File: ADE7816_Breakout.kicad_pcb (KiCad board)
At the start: 2 copper layers, 9 parts, among them J1 Barrel_Jack_Switch, J2 AudioJack3, J3 AudioJack3, J4 AudioJack3, J5 AudioJack3, J6 AudioJack3, J7 AudioJack3, J8 Conn_01x06_Male, U1 ADE7816ACPZ

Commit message: Start adding analog inputs and filters
Signed-off-by: Tisham Dhar <whatnickd@gmail.com>
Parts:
- added C1: 22n, Capacitor_SMD:C_0603_1608Metric, F.Cu at (119.1, 70.1)
- added C10: 22n, Capacitor_SMD:C_0603_1608Metric, F.Cu at (131.5, 42.2)
- added C11: 22n, Capacitor_SMD:C_0603_1608Metric, F.Cu at (127.5, 47.2)
- added C12: 22n, Capacitor_SMD:C_0603_1608Metric, F.Cu at (131.5, 44.7)
- added C13: 22n, Capacitor_SMD:C_0603_1608Metric, F.Cu at (135.5, 42.2)
- added C14: 22n, Capacitor_SMD:C_0603_1608Metric, F.Cu at (-2146.0, -2146.7)
- added C2: 22n, Capacitor_SMD:C_0603_1608Metric, F.Cu at (151.5, 93.9)
- added C3: 22n, Capacitor_SMD:C_0603_1608Metric, F.Cu at (123.1, 70.1)
- added C4: 22n, Capacitor_SMD:C_0603_1608Metric, F.Cu at (119.1, 72.6)
- added C5: 22n, Capacitor_SMD:C_0603_1608Metric, F.Cu at (151.5, 91.4)
- added C6: 22n, Capacitor_SMD:C_0603_1608Metric, F.Cu at (139.3, 85.8)
- added C7: 22n, Capacitor_SMD:C_0603_1608Metric, F.Cu at (155.5, 91.4)
- added C8: 22n, Capacitor_SMD:C_0603_1608Metric, F.Cu at (127.5, 42.2)
- added C9: 22n, Capacitor_SMD:C_0603_1608Metric, F.Cu at (127.5, 44.7)
- added R1: 4.8R, Resistor_SMD:R_0603_1608Metric, F.Cu at (123.4, 67.6)
- added R10: 1k, Resistor_SMD:R_0603_1608Metric, F.Cu at (119.1, 80.1)
- added R11: 1k, Resistor_SMD:R_0603_1608Metric, F.Cu at (127.1, 72.6)
- added R12: 1k, Resistor_SMD:R_0603_1608Metric, F.Cu at (155.5, 93.9)
- added R13: 100k, Resistor_SMD:R_0603_1608Metric_Pad1.05x0.95mm_HandSolder, F.Cu at (119.3, 67.6)
- added R14: 1k, Resistor_SMD:R_0603_1608Metric, F.Cu at (143.3, 85.8)
- added R15: 1k, Resistor_SMD:R_0603_1608Metric, F.Cu at (131.5, 47.2)
- added R16: 1k, Resistor_SMD:R_0603_1608Metric, F.Cu at (135.5, 44.7)
- added R17: 1k, Resistor_SMD:R_0603_1608Metric, F.Cu at (139.5, 42.2)
- added R18: 1k, Resistor_SMD:R_0603_1608Metric, F.Cu at (135.5, 47.2)
- added R19: 1k, Resistor_SMD:R_0603_1608Metric, F.Cu at (139.5, 44.7)
- added R2: 4.8R, Resistor_SMD:R_0603_1608Metric, F.Cu at (123.1, 72.6)
- added R20: 1k, Resistor_SMD:R_0603_1608Metric, F.Cu at (139.5, 47.2)
- added R21: 1k, Resistor_SMD:R_0603_1608Metric, F.Cu at (-2142.0, -2146.7)
- added R3: 4.8R, Resistor_SMD:R_0603_1608Metric, F.Cu at (119.1, 75.1)
- added R4: 4.8R, Resistor_SMD:R_0603_1608Metric, F.Cu at (127.1, 70.1)
- added R5: 4.8R, Resistor_SMD:R_0603_1608Metric, F.Cu at (119.1, 77.6)
- added R6: 4.8R, Resistor_SMD:R_0603_1608Metric, F.Cu at (127.4, 67.6)
- added R7: 1k, Resistor_SMD:R_0603_1608Metric, F.Cu at (139.3, 88.4)
- added R8: 1k, Resistor_SMD:R_0603_1608Metric, F.Cu at (131.5, 67.6)
- added R9: 1k, Resistor_SMD:R_0603_1608Metric, F.Cu at (123.1, 75.1)
- J1: value Barrel_Jack_Switch -> AudioJack3; footprint Connector_BarrelJack:BarrelJack_Horizontal -> Connector_Audio:Jack_3.5mm_CUI_SJ-3523-SMT_Horizontal
- J7: value AudioJack3 -> Barrel_Jack_Switch; footprint Connector_Audio:Jack_3.5mm_CUI_SJ-3523-SMT_Horizontal -> Connector_BarrelJack:BarrelJack_Horizontal
- J8: value Conn_01x06_Male -> Conn_01x10; footprint Connector_PinHeader_2.54mm:PinHeader_1x06_P2.54mm_Vertical -> Connector_PinHeader_2.54mm:PinHeader_1x10_P2.54mm_Vertical
- moved J8 54.9 mm to (157.7, 53.3)
- moved J5 40.3 mm to (101.6, 36.8), turned to 90 degrees
- moved J6 38.2 mm to (101.9, 100.3), turned to 90 degrees
- moved J3 33.1 mm to (101.6, 61.1), turned to 90 degrees
- moved J1 31.2 mm to (101.9, 76.0), turned to 90 degrees
- moved J4 25.3 mm to (101.6, 49.0), turned to 90 degrees
- moved J7 23.0 mm to (128.0, 93.2), turned to 90 degrees
- moved J2 16.8 mm to (101.9, 88.2), turned to 90 degrees
- moved U1 11.8 mm to (136.4, 56.6)
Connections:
- J2 pad R: Net-(J2-PadR) -> (no net)
- J2 pad S: Net-(J2-PadS) -> GNDA
- J3 pad R: Net-(J3-PadR) -> (no net)
- J3 pad S: Net-(J3-PadS) -> GNDA
- J4 pad R: Net-(J4-PadR) -> (no net)
- J4 pad S: Net-(J4-PadS) -> GNDA
- J5 pad R: Net-(J5-PadR) -> (no net)
- J5 pad S: Net-(J5-PadS) -> GNDA
- J6 pad R: Net-(J6-PadR) -> (no net)
- J6 pad S: Net-(J6-PadS) -> GNDA
- J8 pad 1: Net-(J8-Pad1) -> (no net)
- J8 pad 2: Net-(J8-Pad2) -> (no net)
- J8 pad 3: Net-(J8-Pad3) -> (no net)
- J8 pad 4: Net-(J8-Pad4) -> (no net)
- J8 pad 5: Net-(J8-Pad5) -> (no net)
- J8 pad 6: Net-(J8-Pad6) -> (no net)
- U1 pad 1: Net-(U1-Pad1) -> (no net)
- U1 pad 10: Net-(U1-Pad10) -> (no net)
- U1 pad 11: Net-(U1-Pad11) -> (no net)
- U1 pad 12: Net-(U1-Pad12) -> (no net)
- U1 pad 13: Net-(U1-Pad13) -> (no net)
- U1 pad 14: Net-(U1-Pad14) -> (no net)
- U1 pad 15: Net-(U1-Pad15) -> (no net)
- U1 pad 16: Net-(U1-Pad16) -> (no net)
- U1 pad 17: Net-(U1-Pad17) -> (no net)
- U1 pad 18: Net-(U1-Pad18) -> (no net)
- U1 pad 19: Net-(U1-Pad19) -> (no net)
- U1 pad 2: Net-(U1-Pad2) -> (no net)
- U1 pad 20: Net-(U1-Pad20) -> (no net)
- U1 pad 21: Net-(U1-Pad21) -> (no net)
- U1 pad 22: Net-(U1-Pad22) -> (no net)
- U1 pad 23: Net-(U1-Pad23) -> (no net)
- U1 pad 24: Net-(U1-Pad24) -> (no net)
- U1 pad 25: Net-(U1-Pad25) -> (no net)
- U1 pad 26: Net-(U1-Pad26) -> (no net)
- U1 pad 27: Net-(U1-Pad27) -> (no net)
- U1 pad 28: Net-(U1-Pad28) -> (no net)
- U1 pad 29: Net-(U1-Pad29) -> (no net)
- U1 pad 3: Net-(U1-Pad3) -> (no net)
- U1 pad 30: Net-(U1-Pad30) -> (no net)
- U1 pad 31: Net-(U1-Pad31) -> (no net)
- U1 pad 32: Net-(U1-Pad32) -> (no net)
- U1 pad 33: Net-(U1-Pad33) -> (no net)
- U1 pad 34: Net-(U1-Pad34) -> (no net)
- U1 pad 35: Net-(U1-Pad35) -> (no net)
- U1 pad 36: Net-(U1-Pad36) -> (no net)
- U1 pad 37: Net-(U1-Pad37) -> (no net)
- U1 pad 38: Net-(U1-Pad38) -> (no net)
- U1 pad 39: Net-(U1-Pad39) -> (no net)
- U1 pad 4: Net-(U1-Pad4) -> (no net)
- U1 pad 40: Net-(U1-Pad40) -> (no net)
- U1 pad 5: Net-(U1-Pad5) -> (no net)
- U1 pad 6: Net-(U1-Pad6) -> (no net)
- U1 pad 7: Net-(U1-Pad7) -> (no net)
- U1 pad 8: Net-(U1-Pad8) -> (no net)
- U1 pad 9: Net-(U1-Pad9) -> (no net)
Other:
- board outline added: 66 x 76.2 mm

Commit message: Add crystal load caps
Signed-off-by: Tisham Dhar <whatnickd@gmail.com>
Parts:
- added C15: 20p, Capacitor_SMD:C_0603_1608Metric, F.Cu at (128.1, 56.1)
- added C16: 20p, Capacitor_SMD:C_0603_1608Metric, F.Cu at (128.1, 58.6)
- added Y1: 16.384MHz, Crystal:Crystal_SMD_2520-4Pin_2.5x2.0mm, F.Cu at (123.9, 56.9)
- moved C14 3182.6 mm to (143.5, 64.0)
- moved R21 3182.6 mm to (147.5, 64.0)
- moved J8 3.57 mm to (158.0, 56.9)
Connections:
- J1 pad R: (no net) -> Net-(J1-PadR)
- J2 pad R: (no net) -> Net-(J2-PadR)
- J3 pad R: (no net) -> Net-(J3-PadR)
- J4 pad R: (no net) -> Net-(J4-PadR)
- J5 pad R: (no net) -> Net-(J5-PadR)
- J6 pad R: (no net) -> Net-(J6-PadR)
- J7 pad 3: (no net) -> Net-(J7-Pad3)
- J8 pad 1: (no net) -> Net-(J8-Pad1)
- J8 pad 10: (no net) -> Net-(J8-Pad10)
- J8 pad 2: (no net) -> Net-(J8-Pad2)
- J8 pad 3: (no net) -> Net-(J8-Pad3)
- J8 pad 4: (no net) -> Net-(J8-Pad4)
- J8 pad 5: (no net) -> Net-(J8-Pad5)
- J8 pad 6: (no net) -> Net-(J8-Pad6)
- J8 pad 7: (no net) -> Net-(J8-Pad7)
- J8 pad 8: (no net) -> Net-(J8-Pad8)
- J8 pad 9: (no net) -> Net-(J8-Pad9)
- U1 pad 1: (no net) -> Net-(U1-Pad1)
- U1 pad 10: (no net) -> Net-(U1-Pad10)
- U1 pad 11: (no net) -> Net-(U1-Pad11)
- U1 pad 12: (no net) -> Net-(U1-Pad12)
- U1 pad 13: (no net) -> Net-(U1-Pad13)
- U1 pad 14: (no net) -> Net-(U1-Pad14)
- U1 pad 15: (no net) -> Net-(U1-Pad15)
- U1 pad 16: (no net) -> Net-(U1-Pad16)
- U1 pad 17: (no net) -> Net-(U1-Pad17)
- U1 pad 18: (no net) -> Net-(U1-Pad18)
- U1 pad 19: (no net) -> Net-(U1-Pad19)
- U1 pad 2: (no net) -> Net-(U1-Pad2)
- U1 pad 20: (no net) -> Net-(U1-Pad20)
- U1 pad 21: (no net) -> Net-(U1-Pad21)
- U1 pad 22: (no net) -> Net-(U1-Pad22)
- U1 pad 23: (no net) -> Net-(U1-Pad23)
- U1 pad 24: (no net) -> Net-(U1-Pad24)
- U1 pad 25: (no net) -> Net-(U1-Pad25)
- U1 pad 26: (no net) -> Net-(U1-Pad26)
- U1 pad 27: (no net) -> /meter_module/CLKIN
- U1 pad 28: (no net) -> Net-(C15-Pad2)
- U1 pad 29: (no net) -> Net-(U1-Pad29)
- U1 pad 3: (no net) -> Net-(U1-Pad3)
- U1 pad 30: (no net) -> Net-(U1-Pad30)
- U1 pad 31: (no net) -> Net-(U1-Pad31)
- U1 pad 32: (no net) -> Net-(U1-Pad32)
- U1 pad 33: (no net) -> Net-(U1-Pad33)
- U1 pad 34: (no net) -> Net-(U1-Pad34)
- U1 pad 35: (no net) -> Net-(U1-Pad35)
- U1 pad 36: (no net) -> Net-(U1-Pad36)
- U1 pad 37: (no net) -> Net-(U1-Pad37)
- U1 pad 38: (no net) -> Net-(U1-Pad38)
- U1 pad 39: (no net) -> Net-(U1-Pad39)
- U1 pad 4: (no net) -> Net-(U1-Pad4)
- U1 pad 40: (no net) -> Net-(U1-Pad40)
- U1 pad 5: (no net) -> Net-(U1-Pad5)
- U1 pad 6: (no net) -> Net-(U1-Pad6)
- U1 pad 7: (no net) -> Net-(U1-Pad7)
- U1 pad 8: (no net) -> Net-(U1-Pad8)
- U1 pad 9: (no net) -> Net-(U1-Pad9)

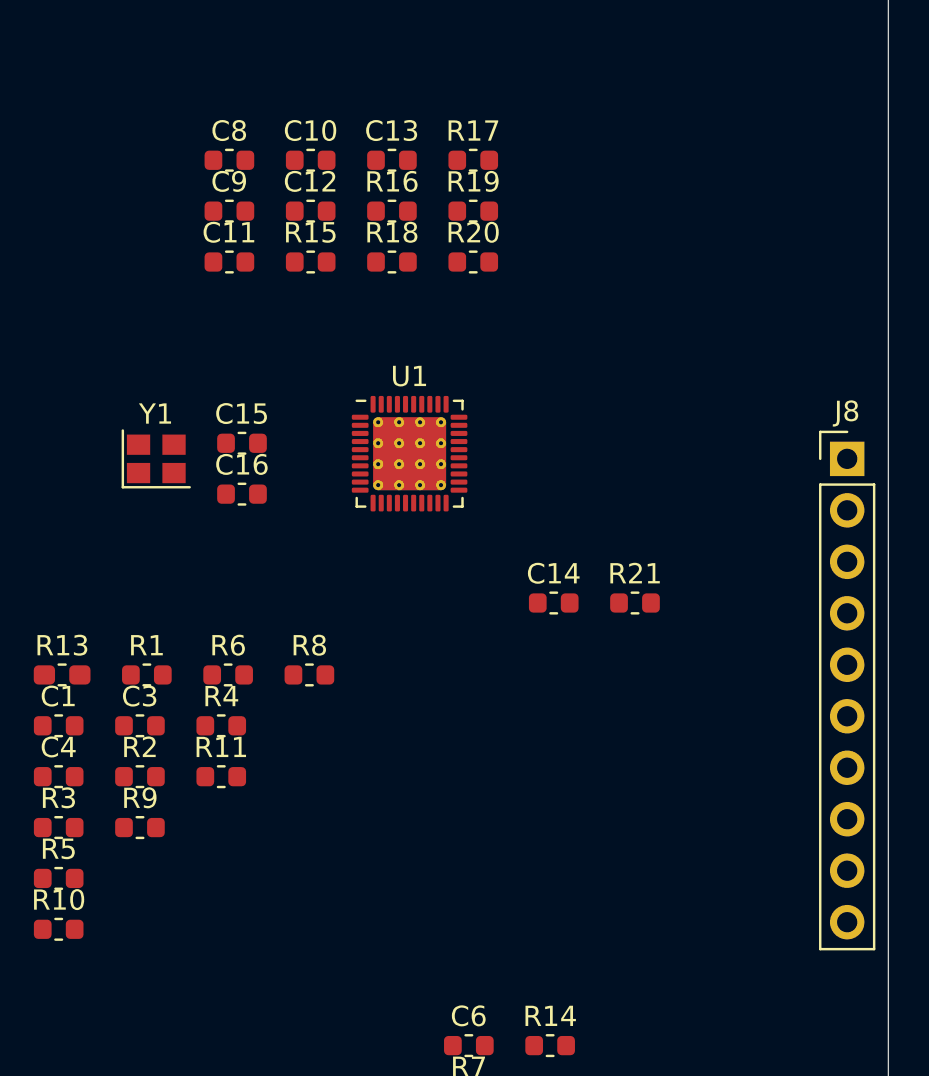
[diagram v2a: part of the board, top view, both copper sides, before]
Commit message: Add more parts and placements
Signed-off-by: Tisham Dhar <whatnickd@gmail.com>
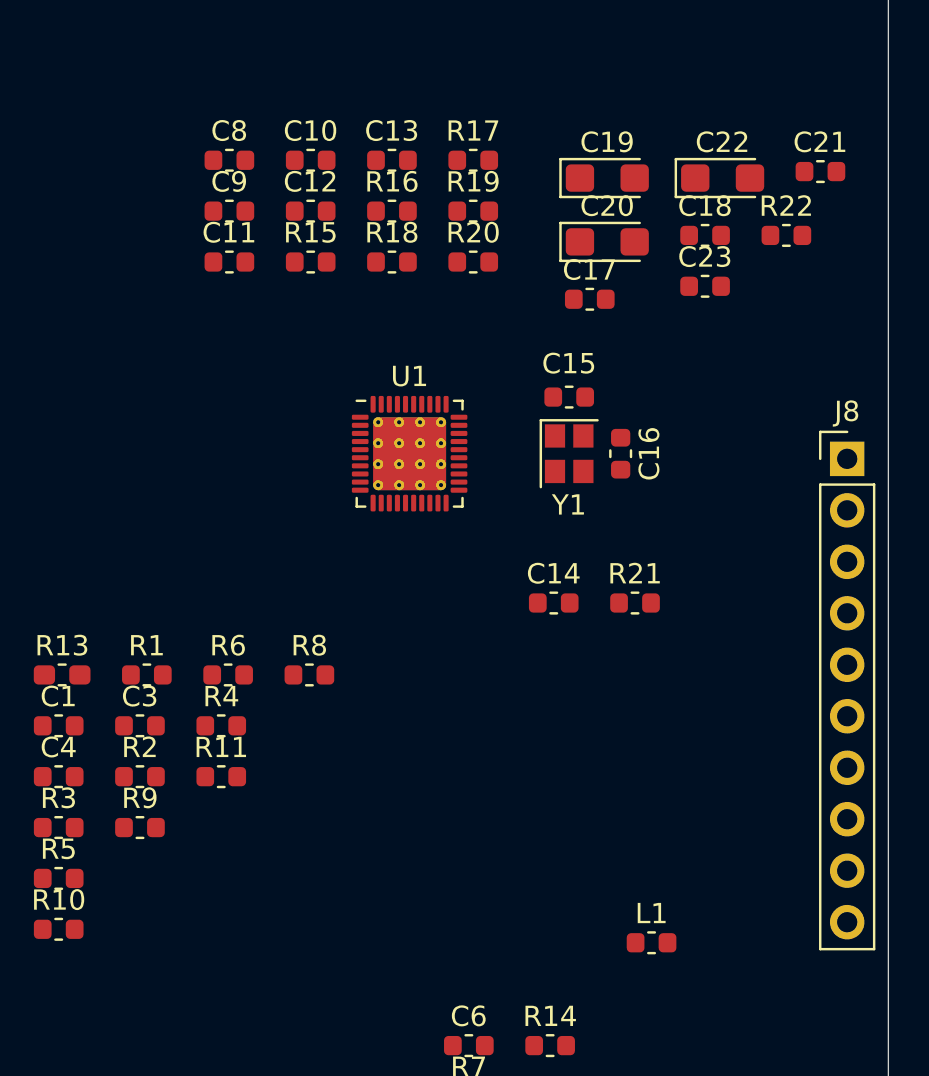
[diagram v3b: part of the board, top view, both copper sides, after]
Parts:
- added C17: 220n, Capacitor_SMD:C_0603_1608Metric, F.Cu at (145.3, 49.0)
- added C18: 220n, Capacitor_SMD:C_0603_1608Metric, F.Cu at (151.0, 45.9)
- added C19: 4.7u, Capacitor_Tantalum_SMD:CP_EIA-3216-18_Kemet-A, F.Cu at (146.2, 43.0)
- added C20: 4.7u, Capacitor_Tantalum_SMD:CP_EIA-3216-18_Kemet-A, F.Cu at (146.2, 46.2)
- added C21: 1u, Capacitor_SMD:C_0603_1608Metric, F.Cu at (156.7, 42.7)
- added C22: 4.7u, Capacitor_Tantalum_SMD:CP_EIA-3216-18_Kemet-A, F.Cu at (151.8, 43.0)
- added C23: 220n, Capacitor_SMD:C_0603_1608Metric, F.Cu at (151.0, 48.4)
- added L1: Ferrite, Inductor_SMD:L_0603_1608Metric, F.Cu at (148.3, 80.8)
- added R22: 10k, Resistor_SMD:R_0603_1608Metric, F.Cu at (155.0, 45.9)
- moved Y1 20.4 mm to (144.3, 56.6), turned to 270 degrees
- moved C16 18.8 mm to (146.8, 56.6), turned to 270 degrees
- moved C15 16.3 mm to (144.3, 53.8), turned to 180 degrees
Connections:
- J8 pad 1: Net-(J8-Pad1) -> /meter_module/~RESET
- J8 pad 10: Net-(J8-Pad10) -> GNDD
- J8 pad 2: Net-(J8-Pad2) -> /meter_module/HSCLK
- J8 pad 3: Net-(J8-Pad3) -> /meter_module/SCLK
- J8 pad 4: Net-(J8-Pad4) -> /meter_module/MOSI
- J8 pad 5: Net-(J8-Pad5) -> /meter_module/MISO
- J8 pad 6: Net-(J8-Pad6) -> /meter_module/~CS
- J8 pad 7: Net-(J8-Pad7) -> /meter_module/~IRQ1
- J8 pad 8: Net-(J8-Pad8) -> /meter_module/~IRQ0
- J8 pad 9: Net-(J8-Pad9) -> +3V3
- U1 pad 2: Net-(U1-Pad2) -> +3V3
- U1 pad 25: Net-(U1-Pad25) -> GNDA
- U1 pad 26: Net-(U1-Pad26) -> +3V3
- U1 pad 29: Net-(U1-Pad29) -> /meter_module/~IRQ0
- U1 pad 3: Net-(U1-Pad3) -> GNDD
- U1 pad 32: Net-(U1-Pad32) -> /meter_module/~IRQ1
- U1 pad 35: Net-(U1-Pad35) -> /meter_module/HSCLK
- U1 pad 36: Net-(U1-Pad36) -> /meter_module/SCLK
- U1 pad 37: Net-(U1-Pad37) -> /meter_module/MISO
- U1 pad 38: Net-(U1-Pad38) -> /meter_module/MOSI
- U1 pad 39: Net-(U1-Pad39) -> /meter_module/~CS
- U1 pad 4: Net-(U1-Pad4) -> /meter_module/~RESET
- U1 pad 41: Net-(U1-Pad41) -> GNDA
- U1 pad 6: Net-(U1-Pad6) -> GNDD

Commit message: Initial round of schematic parts
Signed-off-by: Tisham Dhar <whatnickd@gmail.com>
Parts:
- R1, R2, R3, R4, R5, R6: value 4.8R -> 4.7R
- moved R4 22.6 mm to (113.8, 51.8), turned to 270 degrees
- moved C11 10.6 mm to (117.6, 51.1), turned to 180 degrees
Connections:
- net Net-(C17-Pad1) renamed /meter_module/AVDD
- net Net-(C18-Pad1) renamed /meter_module/DVDD
- C1 pad 1: Net-(C1-Pad1) -> IAP
- C10 pad 1: Net-(C10-Pad1) -> ICN
- C11 pad 1: Net-(C11-Pad1) -> IN
- C14 pad 1: Net-(C14-Pad1) -> VN
- C2 pad 1: Net-(C2-Pad1) -> IBP
- C3 pad 1: Net-(C3-Pad1) -> ICP
- C4 pad 1: Net-(C4-Pad1) -> IDP
- C5 pad 1: Net-(C5-Pad1) -> IEP
- C6 pad 1: Net-(C6-Pad1) -> IFP
- C7 pad 1: Net-(C7-Pad1) -> VP
- C8 pad 1: Net-(C8-Pad1) -> IAN
- C9 pad 1: Net-(C9-Pad1) -> IBN
- R10 pad 1: Net-(C4-Pad1) -> IDP
- R11 pad 1: Net-(C5-Pad1) -> IEP
- R12 pad 1: Net-(C6-Pad1) -> IFP
- R13 pad 1: Net-(C7-Pad1) -> VP
- R14 pad 1: Net-(C7-Pad1) -> VP
- R15 pad 2: Net-(C8-Pad1) -> IAN
- R16 pad 2: Net-(C9-Pad1) -> IBN
- R17 pad 2: Net-(C10-Pad1) -> ICN
- R18 pad 2: Net-(C11-Pad1) -> IN
- R21 pad 1: Net-(C14-Pad1) -> VN
- R7 pad 1: Net-(C1-Pad1) -> IAP
- R8 pad 1: Net-(C2-Pad1) -> IBP
- R9 pad 1: Net-(C3-Pad1) -> ICP
- U1 pad 12: Net-(U1-Pad12) -> IBN
- U1 pad 13: Net-(U1-Pad13) -> ICP
- U1 pad 14: Net-(U1-Pad14) -> ICN
- U1 pad 15: Net-(U1-Pad15) -> VP
- U1 pad 16: Net-(U1-Pad16) -> VN
- U1 pad 18: Net-(U1-Pad18) -> IN
- U1 pad 19: Net-(U1-Pad19) -> IFP
- U1 pad 22: Net-(U1-Pad22) -> IEP
- U1 pad 23: Net-(U1-Pad23) -> IDP
- U1 pad 7: Net-(U1-Pad7) -> IAP
- U1 pad 8: Net-(U1-Pad8) -> IAN
- U1 pad 9: Net-(U1-Pad9) -> IBP

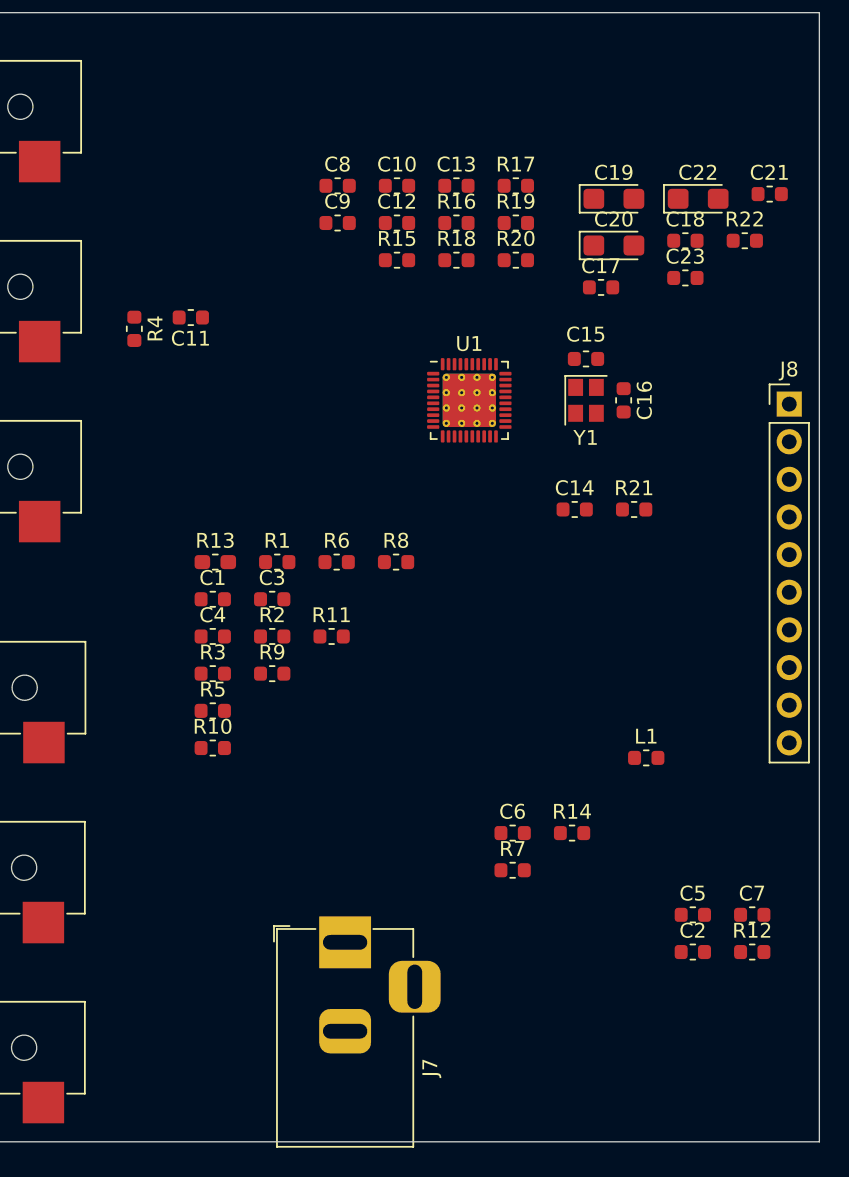
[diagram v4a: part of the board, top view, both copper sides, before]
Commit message: Add part numbers and begin placement
Signed-off-by: Tisham Dhar <whatnickd@gmail.com>
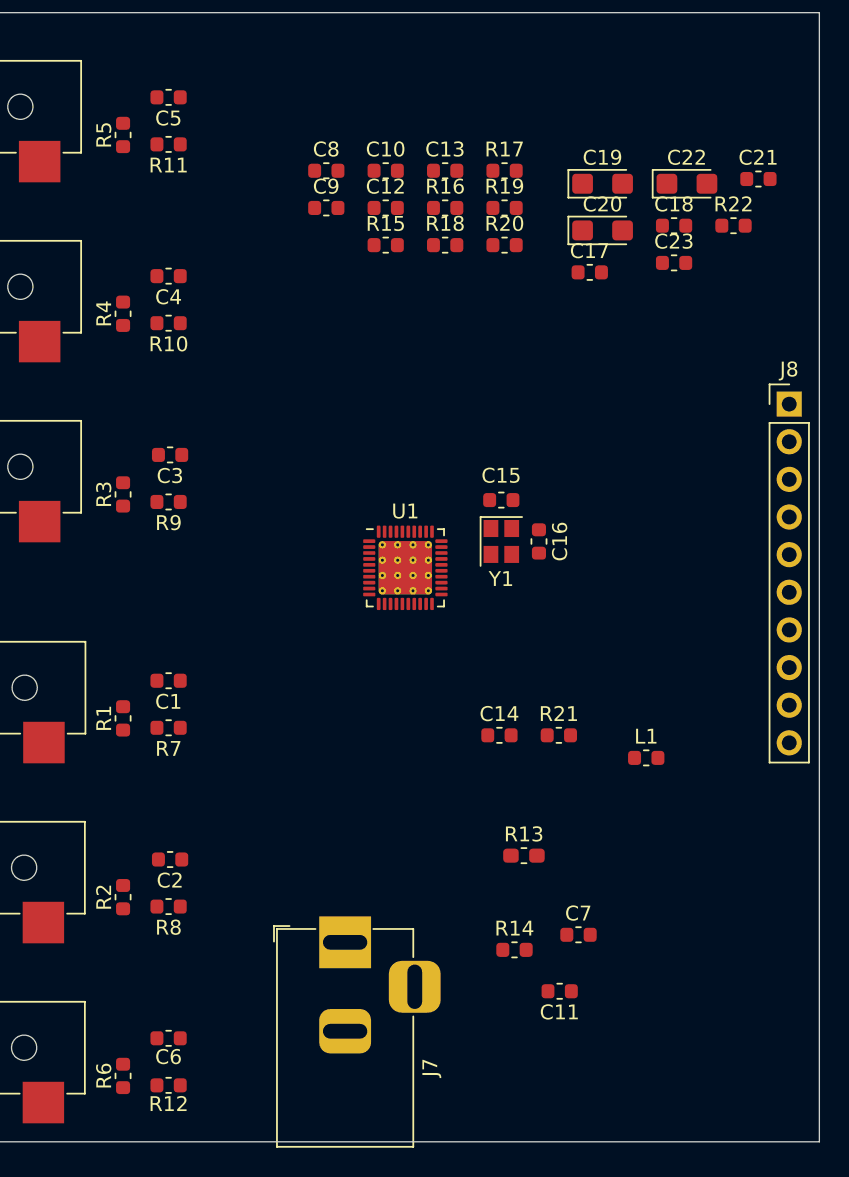
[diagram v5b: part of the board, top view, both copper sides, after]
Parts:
- moved C5 65.5 mm to (116.1, 36.2), turned to 180 degrees
- moved C11 51.8 mm to (142.5, 96.5)
- moved R12 40.4 mm to (116.1, 102.9)
- moved R5 39.3 mm to (113.0, 38.7), turned to 270 degrees
- moved R6 37.6 mm to (113.0, 102.2), turned to 270 degrees
- moved C2 35.8 mm to (116.2, 87.6), turned to 180 degrees
- moved R11 35.0 mm to (116.1, 39.4), turned to 180 degrees
- moved R10 28.8 mm to (116.1, 51.4), turned to 180 degrees
- moved R13 28.7 mm to (140.1, 87.4)
- moved R8 27.9 mm to (116.1, 90.8), turned to 180 degrees
- moved C6 27.0 mm to (116.1, 99.7)
- moved R7 25.1 mm to (116.1, 78.7), turned to 180 degrees
- moved C4 24.5 mm to (116.1, 48.3), turned to 180 degrees
- moved R2 20.3 mm to (113.0, 90.2), turned to 270 degrees
- moved R21 16.1 mm to (142.4, 79.2)
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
